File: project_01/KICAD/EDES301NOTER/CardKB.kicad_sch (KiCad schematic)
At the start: 8 parts, among them Q5 BSS138, Q7 BSS138

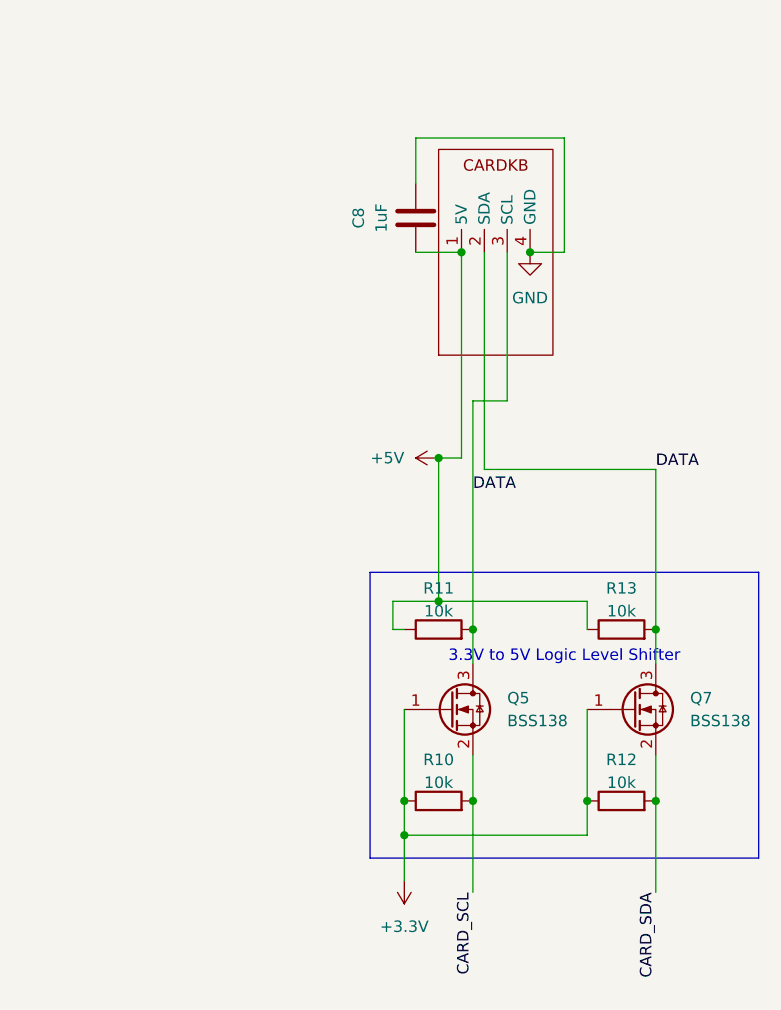
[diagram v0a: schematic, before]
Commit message: Revise Boost5V schematic and add STIKE symbols
Refactor Boost5V.kicad_sch: updated title block and paper size, reorganized and renamed many symbol definitions (capacitor/inductor/diode/resistor/LED/driver), adjusted pin assignments, footprints, datasheet links and symbol graphics. Added new STIKE-related schematic symbols (Slide Switch, LipoConnection) and multiple KiCad footprint/symbol files under KICAD Files. Added project backup zips and freerouting.dsn, removed a temporary .kicad_sch.lck, and updated project metadata files (.kicad_pcb, .kicad_prl, .kicad_pro, .kicad_sch).
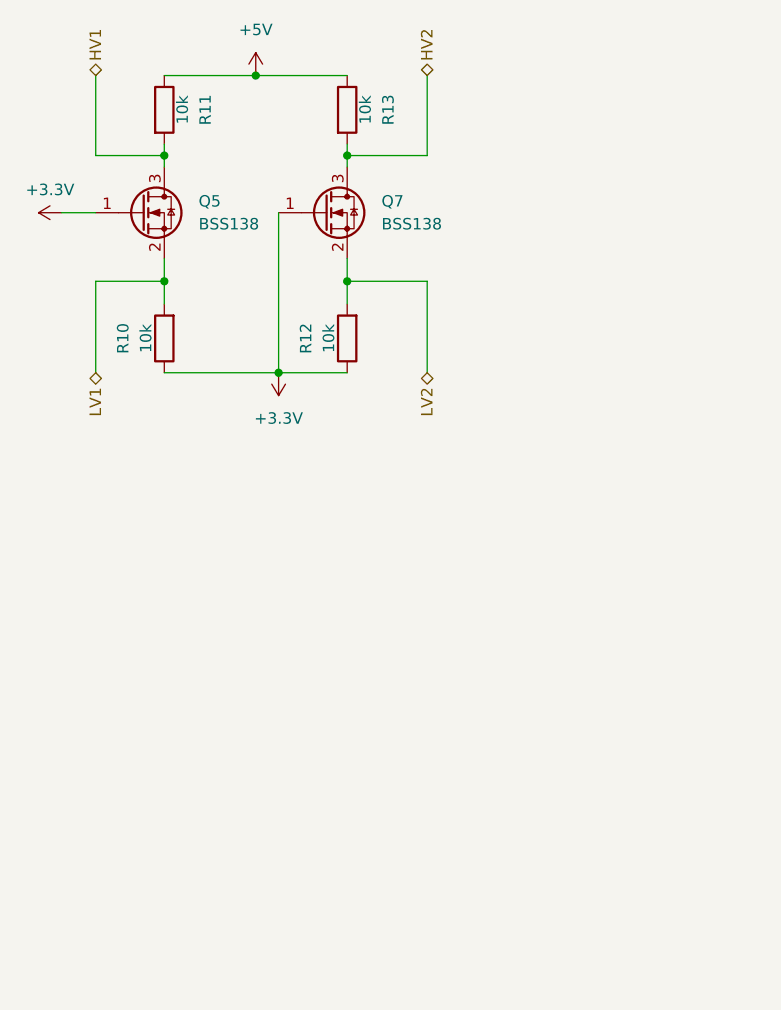
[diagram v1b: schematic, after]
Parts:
- removed C8: 1uF, Footprints:CAPC1608X90N, symbol Device:C
- removed U4: ~, HomeBrew:4_Wire_Connector, symbol STIKE:CARDKB
- R10, R11, R12, R13: footprint Footprints:RESC1607X60N -> Resistor_SMD:R_0603_1608Metric_Pad0.98x0.95mm_HandSolder
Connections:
- net CARD_SCL renamed LV1
- net CARD_SDA renamed LV2
- net DATA renamed HV1
- net HV1: no longer Q7.3 (D), R13.2
- new net HV2: Q7.3 (D), R13.2
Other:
- note removed: "3.3V to 5V Logic Level Shifter"
- title: CardKB Support Circuitry -> STIK eNote
- moved on the sheet: Q5, Q7, R10, R11, R12, R13
